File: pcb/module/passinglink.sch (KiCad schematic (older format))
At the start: 47 parts, among them J1 Conn_01x05_Female, J10 Conn_02x04_Odd_Even, J11 Conn_01x01, J12 Conn_01x04, J2 Conn_01x04, J3 Conn_02x05_Odd_Even, J4 Conn_01x05, J5 Conn_01x05, J6 Conn_02x08_Odd_Even, J7 Conn_02x08_Odd_Even, J8 Conn_01x03, J9 Conn_01x03, U1 STM32F103RETx, U2 MIC5219-3.3YM5, X1 PCB-USB-C, Y1 Crystal_GND2_Small

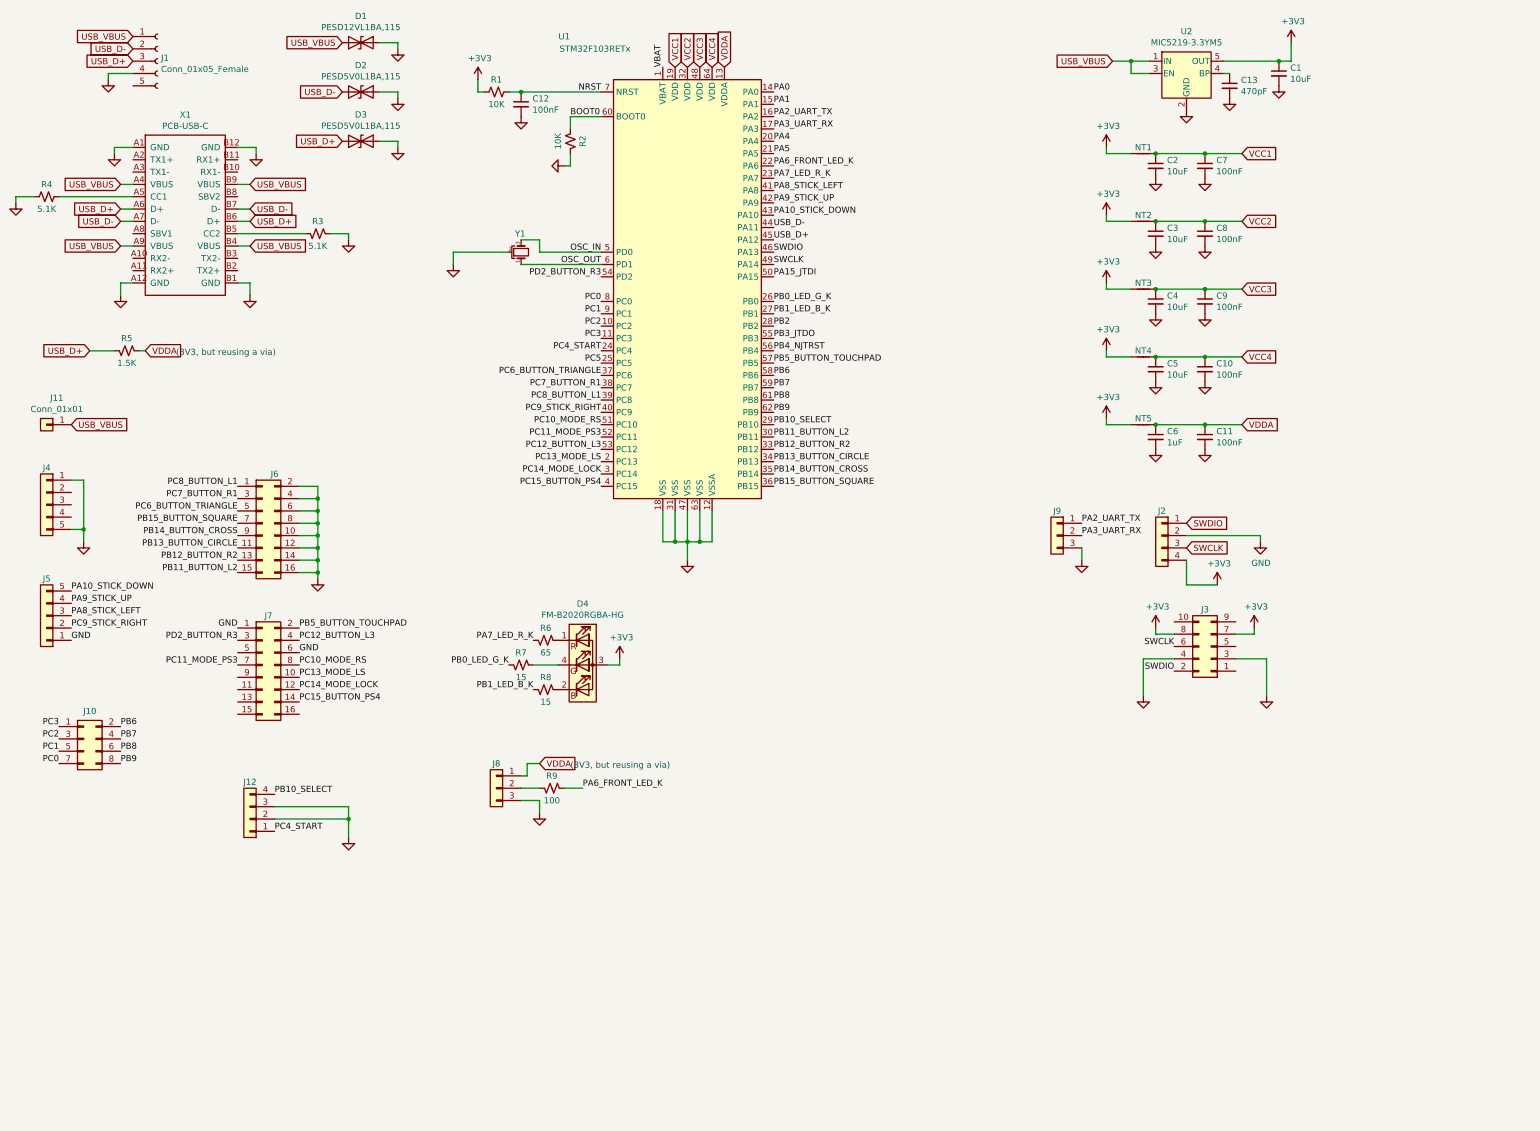
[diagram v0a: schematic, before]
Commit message: PCB v0.5.
Layout a new PCB that connects to an external breakout board via an M.2
connector.
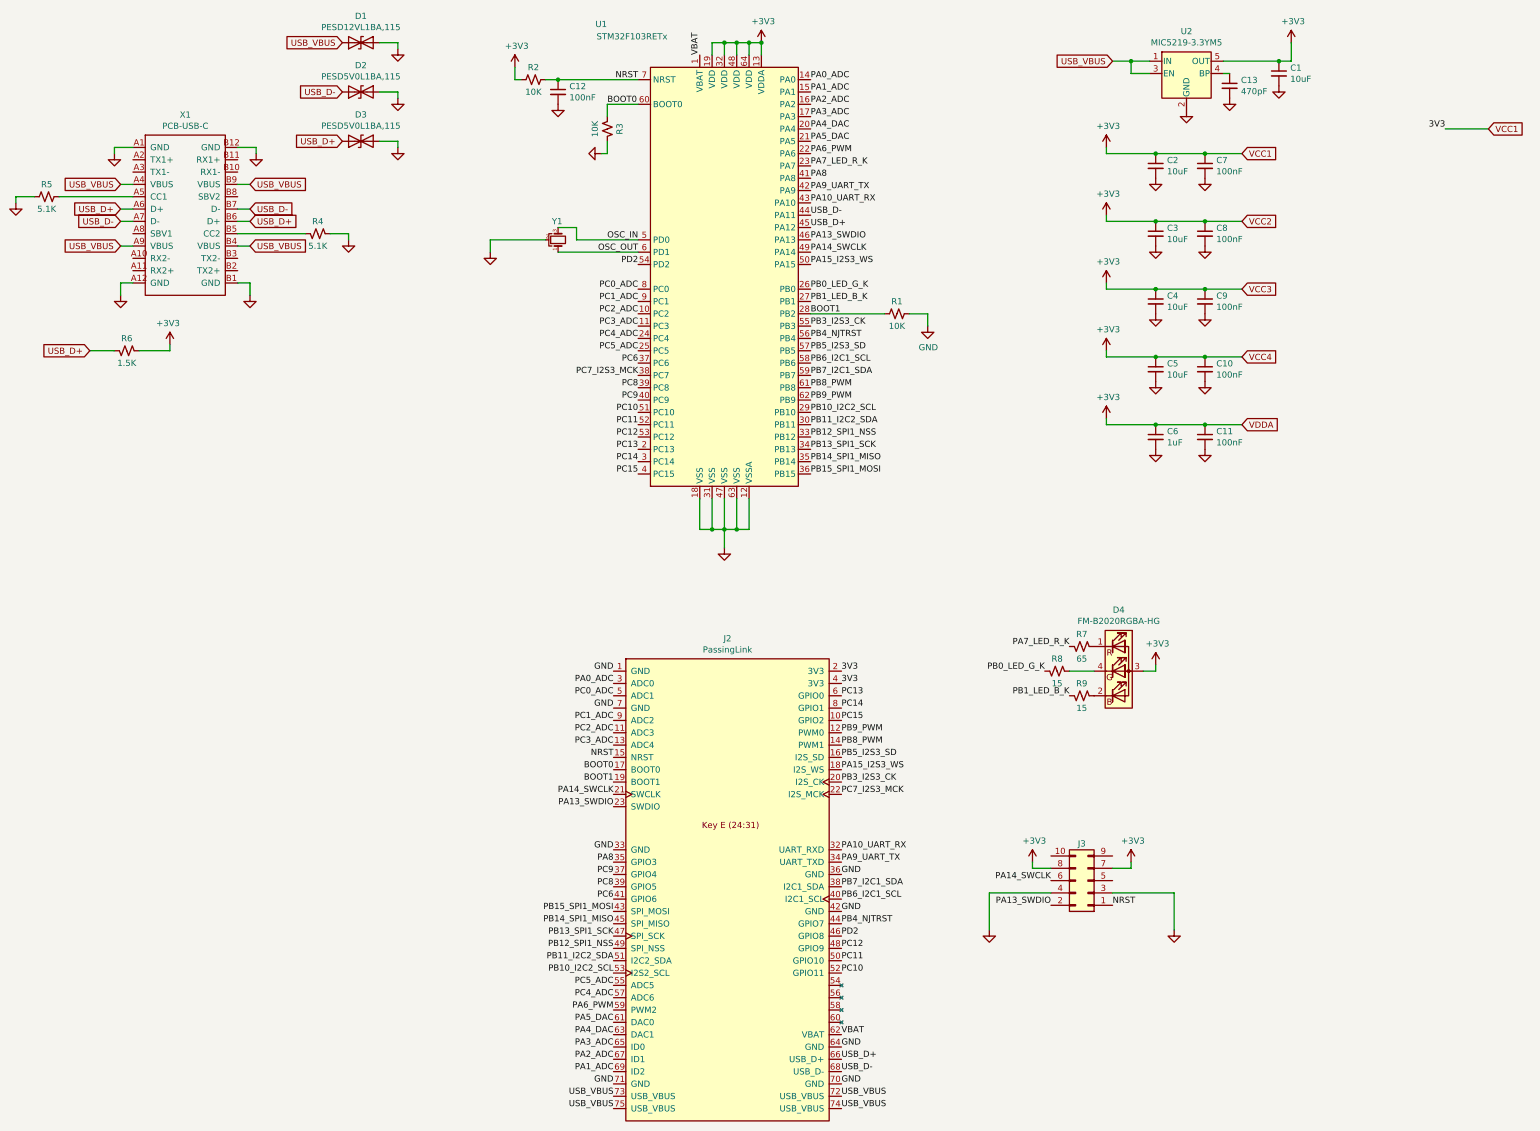
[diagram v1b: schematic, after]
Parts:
- removed J1: Conn_01x05_Female, Connector_JST:JST_XH_B5B-XH-A_1x05_P2.50mm_Vertical, symbol Connector:Conn_01x05_Female
- removed J10: Conn_02x04_Odd_Even, Connector_PinHeader_1.27mm:PinHeader_2x04_P1.27mm_Vertical, symbol Connector_Generic:Conn_02x04_Odd_Even
- removed J11: Conn_01x01, Connector_PinHeader_2.54mm:PinHeader_1x01_P2.54mm_Vertical, symbol Connector_Generic:Conn_01x01
- removed J12: Conn_01x04, Connector_JST:JST_XH_B4B-XH-A_1x04_P2.50mm_Vertical, symbol Connector_Generic:Conn_01x04
- removed J2: Conn_01x04, Connector_PinHeader_2.54mm:PinHeader_1x04_P2.54mm_Vertical, symbol Connector_Generic:Conn_01x04
- removed J4, J5: Conn_01x05, Connector_JST:JST_XH_B5B-XH-A_1x05_P2.50mm_Vertical, symbol Connector_Generic:Conn_01x05
- removed J6, J7: Conn_02x08_Odd_Even, Connector_PinHeader_2.54mm:PinHeader_2x08_P2.54mm_Vertical, symbol Connector_Generic:Conn_02x08_Odd_Even
- removed J8, J9: Conn_01x03, Connector_JST:JST_XH_B3B-XH-A_1x03_P2.50mm_Vertical, symbol Connector_Generic:Conn_01x03
- removed NT1, NT2, NT3, NT4, NT5: Net-Tie_2, NetTie:NetTie-2_SMD_Pad0.5mm, symbol Device:Net-Tie_2
- removed R9: 100, Resistor_SMD:R_0603_1608Metric, symbol Device:R_Small_US
- added J2: PassingLink, NGFF:NGFF_E, symbol passinglink:PassingLink
- added R1: 10K, Resistor_SMD:R_0603_1608Metric, symbol Device:R_Small_US
- renumbered R1 to R2, R2 to R3, R3 to R4, R4 to R5, R5 to R6, R6 to R7, R7 to R8, R8 to R9
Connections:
- net VCC1 is gone; now on net +3V3: C2.1, C7.1, U1.19 (VDD)
- net VCC2 is gone; now on net +3V3: C3.1, C8.1, U1.32 (VDD)
- net VCC3 is gone; now on net +3V3: C4.1, C9.1, U1.48 (VDD)
- net VCC4 is gone; now on net +3V3: C10.1, C5.1, U1.64 (VDD)
- net VDDA is gone; now on net +3V3: C11.1, C6.1, R6.2, U1.13 (VDDA)
- net +3V3: now also J2.2 (3V3), J2.4 (3V3)
- net BOOT0: now also J2.17 (BOOT0)
- net GND: now also J2.1 (GND), J2.33 (GND), J2.36 (GND), J2.42 (GND), J2.64 (GND), J2.7 (GND), J2.70 (GND), J2.71 (GND), R1.1
- net NRST: now also J3.1 (Pin_1), J2.15 (NRST)
- net PB4_NJTRST: now also J2.44 (GPIO7)
- net USB_D+: now also J2.66 (USB_D+)
- net USB_D-: now also J2.68 (USB_D-)
- net USB_VBUS: now also J2.72 (USB_VBUS), J2.73 (USB_VBUS), J2.74 (USB_VBUS), J2.75 (USB_VBUS)
- net VBAT: now also J2.62 (VBAT)
- net PA0 renamed PA0_ADC
- net PA0_ADC: now also J2.3 (ADC0)
- net PA1 renamed PA1_ADC
- net PA1_ADC: now also J2.69 (ID2)
- net PA10_STICK_DOWN renamed PA10_UART_RX
- net PA10_UART_RX: now also J2.32 (UART_RXD)
- net PA15_JTDI renamed PA15_I2S3_WS
- net PA15_I2S3_WS: now also J2.18 (I2S_WS)
- net PA2_UART_TX renamed PA2_ADC
- net PA2_ADC: now also J2.67 (ID1)
- net PA3_UART_RX renamed PA3_ADC
- net PA3_ADC: now also J2.65 (ID0)
- net PA4 renamed PA4_DAC
- net PA4_DAC: now also J2.63 (DAC1)
- net PA5 renamed PA5_DAC
- net PA5_DAC: now also J2.61 (DAC0)
- net PA6_FRONT_LED_K renamed PA6_PWM
- net PA6_PWM: now also J2.59 (PWM2)
- net PA8_STICK_LEFT renamed PA8
- net PA8: now also J2.35 (GPIO3)
- net PA9_STICK_UP renamed PA9_UART_TX
- net PA9_UART_TX: now also J2.34 (UART_TXD)
- net PB10_SELECT renamed PB10_I2C2_SCL
- net PB10_I2C2_SCL: now also J2.53 (I2S2_SCL)
- net PB11_BUTTON_L2 renamed PB11_I2C2_SDA
- net PB11_I2C2_SDA: now also J2.51 (I2C2_SDA)
- net PB12_BUTTON_R2 renamed PB12_SPI1_NSS
- net PB12_SPI1_NSS: now also J2.49 (SPI_NSS)
- net PB13_BUTTON_CIRCLE renamed PB13_SPI1_SCK
- net PB13_SPI1_SCK: now also J2.47 (SPI_SCK)
- net PB14_BUTTON_CROSS renamed PB14_SPI1_MISO
- net PB14_SPI1_MISO: now also J2.45 (SPI_MISO)
- net PB15_BUTTON_SQUARE renamed PB15_SPI1_MOSI
- net PB15_SPI1_MOSI: now also J2.43 (SPI_MOSI)
- net PB2 renamed BOOT1
- net BOOT1: now also J2.19 (BOOT1), R1.2
- net PB3_JTDO renamed PB3_I2S3_CK
- net PB3_I2S3_CK: now also J2.20 (I2S_CK)
- net PB5_BUTTON_TOUCHPAD renamed PB5_I2S3_SD
- net PB5_I2S3_SD: now also J2.16 (I2S_SD)
- net PB6 renamed PB6_I2C1_SCL
- net PB6_I2C1_SCL: now also J2.40 (I2C1_SCL)
- net PB7 renamed PB7_I2C1_SDA
- net PB7_I2C1_SDA: now also J2.38 (I2C1_SDA)
- net PB8 renamed PB8_PWM
- net PB8_PWM: now also J2.14 (PWM1)
- net PB9 renamed PB9_PWM
- net PB9_PWM: now also J2.12 (PWM0)
- net PC0 renamed PC0_ADC
- net PC0_ADC: now also J2.5 (ADC1)
- net PC1 renamed PC1_ADC
- net PC1_ADC: now also J2.9 (ADC2)
- net PC10_MODE_RS renamed PC10
- net PC10: now also J2.52 (GPIO11)
- net PC11_MODE_PS3 renamed PC11
- net PC11: now also J2.50 (GPIO10)
- net PC12_BUTTON_L3 renamed PC12
- net PC12: now also J2.48 (GPIO9)
- net PC13_MODE_LS renamed PC13
- net PC13: now also J2.6 (GPIO0)
- net PC14_MODE_LOCK renamed PC14
- net PC14: now also J2.8 (GPIO1)
- net PC15_BUTTON_PS4 renamed PC15
- net PC15: now also J2.10 (GPIO2)
- net PC2 renamed PC2_ADC
- net PC2_ADC: now also J2.11 (ADC3)
- net PC3 renamed PC3_ADC
- net PC3_ADC: now also J2.13 (ADC4)
- net PC4_START renamed PC4_ADC
- net PC4_ADC: now also J2.57 (ADC6)
- net PC5 renamed PC5_ADC
- net PC5_ADC: now also J2.55 (ADC5)
- net PC6_BUTTON_TRIANGLE renamed PC6
- net PC6: now also J2.41 (GPIO6)
- net PC7_BUTTON_R1 renamed PC7_I2S3_MCK
- net PC7_I2S3_MCK: now also J2.22 (I2S_MCK)
- net PC8_BUTTON_L1 renamed PC8
- net PC8: now also J2.39 (GPIO5)
- net PC9_STICK_RIGHT renamed PC9
- net PC9: now also J2.37 (GPIO4)
- net PD2_BUTTON_R3 renamed PD2
- net PD2: now also J2.46 (GPIO8)
- net SWCLK renamed PA14_SWCLK
- net PA14_SWCLK: now also J2.21 (SWCLK)
- net SWDIO renamed PA13_SWDIO
- net PA13_SWDIO: now also J2.23 (SWDIO)
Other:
- note removed: "(3V3, but reusing a via)"
- moved on the sheet: C12, D4, J3, R2, R3, R7, R8, R9, U1, Y1
